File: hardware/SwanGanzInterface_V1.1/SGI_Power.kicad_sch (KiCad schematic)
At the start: 24 parts, among them IC1 LM2937ESX-3.3_NOPB, J1 Conn_01x02_Pin, Q1 SQ2389CES-T1_GE3, SW1 Power_Switch, U1 LM4041CILPR, U2 OPA2350, U3 OPA2350

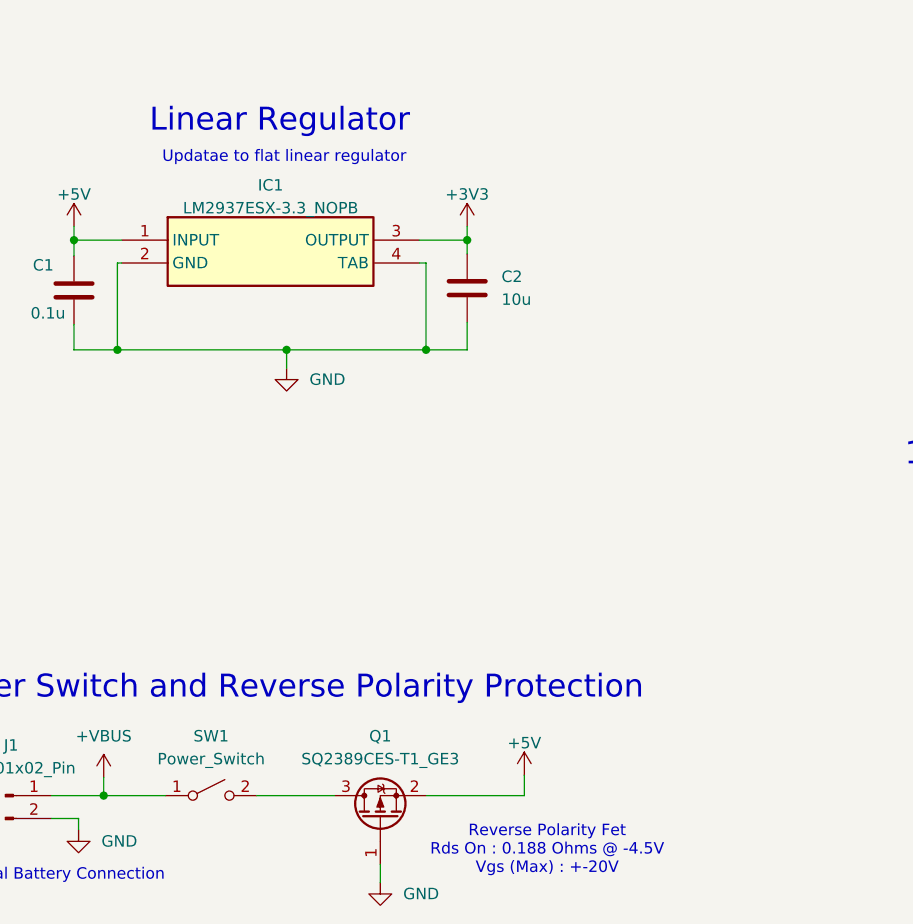
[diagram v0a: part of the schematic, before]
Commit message: Layout work on screen and expanded board size
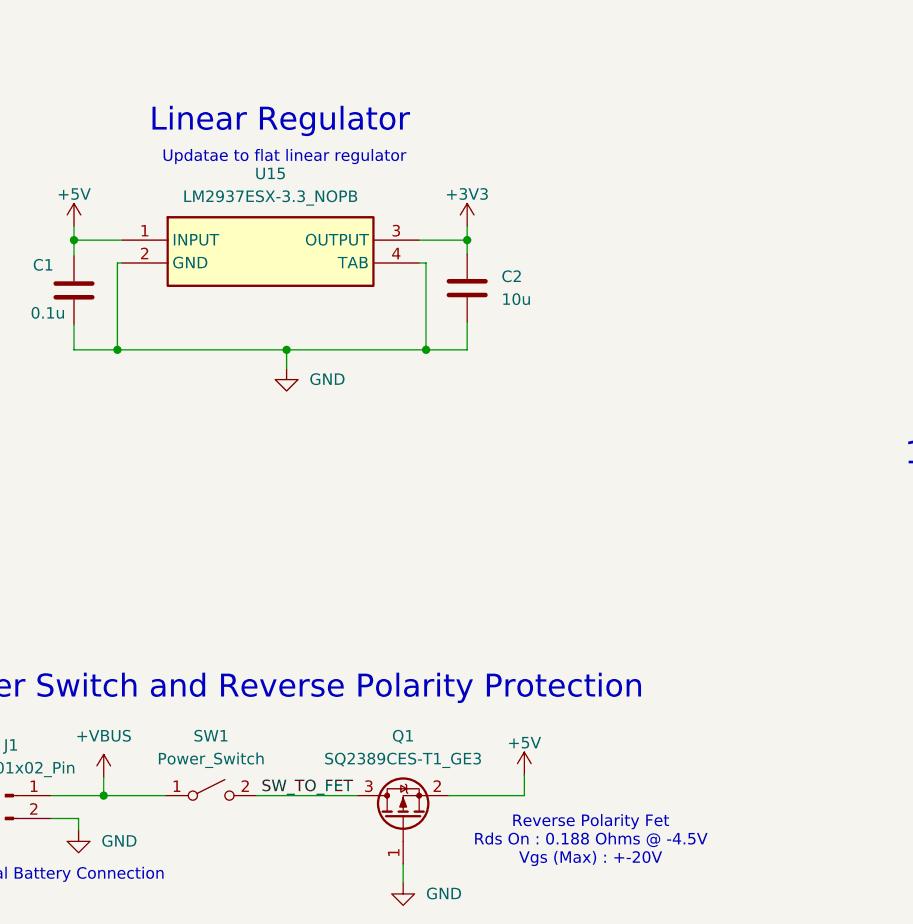
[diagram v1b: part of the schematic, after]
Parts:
- renumbered IC1 to U15
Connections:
- net SW_TO_FET: now reaches Q1.3 (D), SW1.2 (B)
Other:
- moved on the sheet: Q1
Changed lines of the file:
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@@
 	(text "Reverse Polarity Fet\nRds On : 0.188 Ohms @ -4.5V\nVgs (Max) : +-20V"
 		(exclude_from_sim no)
-		(at 89.154 185.674 0)
+		(at 93.98 184.658 0)
 		(effects
 			(font
@@
 	(wire
 		(pts
-			(xy 70.612 189.23) (xy 70.612 187.198)
-		)
-		(stroke
-			(width 0)
-			(type default)
-		)
-	)
-	(wire
-		(pts
 			(xy 232.918 111.252) (xy 235.712 111.252)
 		)
@@
 	(wire
 		(pts
-			(xy 75.692 179.578) (xy 86.614 179.578)
+			(xy 78.232 179.578) (xy 86.614 179.578)
 		)
 		(stroke
@@
 	(wire
 		(pts
-			(xy 56.896 179.578) (xy 65.532 179.578)
+			(xy 56.896 179.578) (xy 68.072 179.578)
 		)
 		(stroke
@@
 	(wire
 		(pts
+			(xy 73.152 187.198) (xy 73.152 189.23)
+		)
+		(stroke
+			(width 0)
+			(type default)
+		)
+	)
+	(wire
+		(pts
 			(xy 150.114 160.528) (xy 157.734 160.528)
 		)
@@
 		)
 	)
-	(global_label "Touch_VRef"
-		(shape output)
-		(at 235.712 111.252 0)
-		(fields_autoplaced yes)
+	(label "SW_TO_FET"
+		(at 57.404 179.578 0)
 		(effects
 			(font
 				(size 1.27 1.27)
 			)
-			(justify left)
-		)
-		(property "Intersheetrefs" "${INTERSHEET_REFS}"
-			(at 249.3409 111.252 0)
-			(effects
-				(font
-					(size 1.27 1.27)
-				)
-				(justify left)
-				(hide yes)
-			)
+			(justify left bottom)
 		)
 	)
@@
 		)
 	)
+	(global_label "Touch_VRef"
+		(shape output)
+		(at 235.712 111.252 0)
+		(fields_autoplaced yes)
+		(effects
+			(font
+				(size 1.27 1.27)
+			)
+			(justify left)
+		)
+		(property "Intersheetrefs" "${INTERSHEET_REFS}"
+			(at 249.3409 111.252 0)
+			(effects
+				(font
+					(size 1.27 1.27)
+				)
+				(justify left)
+				(hide yes)
+			)
+		)
+	)
 	(global_label "+VRef"
 		(shape input)
@@
 	(symbol
 		(lib_id "SGI_SymbolLib:SQ2389CES-T1_GE3")
-		(at 70.612 182.118 90)
+		(at 73.152 182.118 90)
 		(unit 1)
 		(exclude_from_sim no)
@@
 		(dnp no)
 		(property "Reference" "Q1"
-			(at 70.612 172.974 90)
+			(at 73.152 172.974 90)
 			(effects
 				(font
@@
 		)
 		(property "Value" "SQ2389CES-T1_GE3"
-			(at 70.612 175.514 90)
+			(at 73.152 175.514 90)
 			(effects
 				(font
@@
 		)
 		(property "Footprint" "Package_TO_SOT_SMD:SOT-23"
-			(at 72.517 177.038 0)
+			(at 75.057 177.038 0)
 			(effects
 				(font
@@
 		)
 		(property "Datasheet" "kicad-embed://sq2389ces.pdf"
-			(at 74.422 177.038 0)
+			(at 76.962 177.038 0)
 			(effects
 				(font
@@
 		)
 		(property "Description" "-0.18A Id, -60V Vds, P-Channel MOSFET, SOT-23"
-			(at 70.612 182.118 0)
+			(at 73.152 182.118 0)
 			(effects
 				(font
@@
 	(symbol
 		(lib_id "power:GNDA")
-		(at 70.612 189.23 0)
+		(at 73.152 189.23 0)
 		(unit 1)
 		(exclude_from_sim no)
@@
 		(fields_autoplaced yes)
 		(property "Reference" "#PWR04"
-			(at 70.612 195.58 0)
+			(at 73.152 195.58 0)
 			(effects
 				(font
@@
 		)
 		(property "Value" "GND"
-			(at 73.152 190.4999 0)
+			(at 75.692 190.4999 0)
 			(effects
 				(font
@@
 		)
 		(property "Footprint" ""
-			(at 70.612 189.23 0)
+			(at 73.152 189.23 0)
 			(effects
 				(font
@@
 		)
 		(property "Datasheet" ""
-			(at 70.612 189.23 0)
+			(at 73.152 189.23 0)
 			(effects
 				(font
@@
 		)
 		(property "Description" "Power symbol creates a global label with name \"GNDA\" , analog ground"
-			(at 70.612 189.23 0)
+			(at 73.152 189.23 0)
 			(effects
 				(font
@@
 		(dnp no)
 		(fields_autoplaced yes)
-		(property "Reference" "IC1"
-			(at 58.42 111.76 0)
+		(property "Reference" "U15"
+			(at 58.42 110.49 0)
 			(effects
 				(font
@@
 		)
 		(property "Value" "LM2937ESX-3.3_NOPB"
-			(at 58.42 114.3 0)
+			(at 58.42 113.03 0)
 			(effects
 				(font
@@
 			(project ""
 				(path "/4e9a6e30-f660-472b-9696-bea1f34b4545/090a1e64-9482-4912-b352-6eea35714559"
-					(reference "IC1")
+					(reference "U15")
 					(unit 1)
 				)

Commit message: SGI v2 Layout Complete
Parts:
- renumbered U15 to U1, U1 to U2, U2 to U3, U3 to U4
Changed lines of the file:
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@@
 		(on_board yes)
 		(dnp no)
-		(property "Reference" "U3"
+		(property "Reference" "U4"
 			(at 223.266 86.36 0)
 			(effects
@@
 			(project ""
 				(path "/4e9a6e30-f660-472b-9696-bea1f34b4545/090a1e64-9482-4912-b352-6eea35714559"
-					(reference "U3")
+					(reference "U4")
 					(unit 1)
 				)
@@
 		(dnp no)
 		(fields_autoplaced yes)
-		(property "Reference" "#PWR01"
+		(property "Reference" "#PWR02"
 			(at 37.084 189.738 0)
 			(effects
@@
 			(project "SwanGanzInterface_V1.1"
 				(path "/4e9a6e30-f660-472b-9696-bea1f34b4545/090a1e64-9482-4912-b352-6eea35714559"
-					(reference "#PWR01")
+					(reference "#PWR02")
 					(unit 1)
 				)
@@
 		(dnp no)
 		(fields_autoplaced yes)
-		(property "Reference" "U2"
+		(property "Reference" "U3"
 			(at 222.758 60.071 0)
 			(effects
@@
 			(project ""
 				(path "/4e9a6e30-f660-472b-9696-bea1f34b4545/090a1e64-9482-4912-b352-6eea35714559"
-					(reference "U2")
+					(reference "U3")
 					(unit 2)
 				)
@@
 		(dnp no)
 		(fields_autoplaced yes)
-		(property "Reference" "#PWR02"
+		(property "Reference" "#PWR03"
 			(at 39.878 181.356 0)
 			(effects
@@
 			(project ""
 				(path "/4e9a6e30-f660-472b-9696-bea1f34b4545/090a1e64-9482-4912-b352-6eea35714559"
-					(reference "#PWR02")
+					(reference "#PWR03")
 					(unit 1)
 				)
@@
 		(dnp no)
 		(fields_autoplaced yes)
-		(property "Reference" "U1"
+		(property "Reference" "U2"
 			(at 152.654 170.8784 0)
 			(effects
@@
 			(project ""
 				(path "/4e9a6e30-f660-472b-9696-bea1f34b4545/090a1e64-9482-4912-b352-6eea35714559"
-					(reference "U1")
+					(reference "U2")
 					(unit 1)
 				)
@@
 		(dnp no)
 		(fields_autoplaced yes)
-		(property "Reference" "#PWR04"
+		(property "Reference" "#PWR05"
 			(at 73.152 195.58 0)
 			(effects
@@
 			(project "SwanGanzInterface"
 				(path "/4e9a6e30-f660-472b-9696-bea1f34b4545/090a1e64-9482-4912-b352-6eea35714559"
-					(reference "#PWR04")
+					(reference "#PWR05")
 					(unit 1)
 				)
@@
 		(dnp no)
 		(fields_autoplaced yes)
-		(property "Reference" "U15"
+		(property "Reference" "U1"
 			(at 58.42 110.49 0)
 			(effects
@@
 			(project ""
 				(path "/4e9a6e30-f660-472b-9696-bea1f34b4545/090a1e64-9482-4912-b352-6eea35714559"
-					(reference "U15")
+					(reference "U1")
 					(unit 1)
 				)
@@
 		(on_board yes)
 		(dnp no)
-		(property "Reference" "#PWR03"
+		(property "Reference" "#PWR01"
 			(at 36.576 120.142 0)
 			(effects
@@
 			(project "SwanGanzInterface"
 				(path "/4e9a6e30-f660-472b-9696-bea1f34b4545/090a1e64-9482-4912-b352-6eea35714559"
-					(reference "#PWR03")
+					(reference "#PWR01")
 					(unit 1)
 				)
@@
 		(on_board yes)
 		(dnp no)
-		(property "Reference" "#PWR06"
+		(property "Reference" "#PWR07"
 			(at 86.614 181.102 0)
 			(effects
@@
 			(project "SwanGanzInterface"
 				(path "/4e9a6e30-f660-472b-9696-bea1f34b4545/090a1e64-9482-4912-b352-6eea35714559"
-					(reference "#PWR06")
+					(reference "#PWR07")
 					(unit 1)
 				)
@@
 		(on_board yes)
 		(dnp no)
-		(property "Reference" "U3"
+		(property "Reference" "U4"
 			(at 225.552 105.41 0)
 			(effects
@@
 			(project ""
 				(path "/4e9a6e30-f660-472b-9696-bea1f34b4545/090a1e64-9482-4912-b352-6eea35714559"
-					(reference "U3")
+					(reference "U4")
 					(unit 2)
 				)
@@
 		(on_board yes)
 		(dnp no)
-		(property "Reference" "U2"
+		(property "Reference" "U3"
 			(at 266.065 61.9759 0)
 			(effects
@@
 			(project ""
 				(path "/4e9a6e30-f660-472b-9696-bea1f34b4545/090a1e64-9482-4912-b352-6eea35714559"
-					(reference "U2")
+					(reference "U3")
 					(unit 3)
 				)
@@
 		(on_board yes)
 		(dnp no)
-		(property "Reference" "#PWR07"
+		(property "Reference" "#PWR06"
 			(at 80.264 120.142 0)
 			(effects
@@
 			(project "SwanGanzInterface"
 				(path "/4e9a6e30-f660-472b-9696-bea1f34b4545/090a1e64-9482-4912-b352-6eea35714559"
-					(reference "#PWR07")
+					(reference "#PWR06")
 					(unit 1)
 				)
@@
 		(on_board yes)
 		(dnp no)
-		(property "Reference" "U3"
+		(property "Reference" "U4"
 			(at 266.192 96.7739 0)
 			(effects
@@
 			(project ""
 				(path "/4e9a6e30-f660-472b-9696-bea1f34b4545/090a1e64-9482-4912-b352-6eea35714559"
-					(reference "U3")
+					(reference "U4")
 					(unit 3)
 				)
@@
 		(dnp no)
 		(fields_autoplaced yes)
-		(property "Reference" "#PWR05"
+		(property "Reference" "#PWR04"
 			(at 60.198 138.43 0)
 			(effects
@@
 			(project ""
 				(path "/4e9a6e30-f660-472b-9696-bea1f34b4545/090a1e64-9482-4912-b352-6eea35714559"
-					(reference "#PWR05")
+					(reference "#PWR04")
 					(unit 1)
 				)
@@
 		(dnp no)
 		(fields_autoplaced yes)
-		(property "Reference" "U2"
+		(property "Reference" "U3"
 			(at 222.758 38.354 0)
 			(effects
@@
 			(project ""
 				(path "/4e9a6e30-f660-472b-9696-bea1f34b4545/090a1e64-9482-4912-b352-6eea35714559"
-					(reference "U2")
-					(unit 1)
-				)
+					(reference "U3")
+					(unit 1)
+				)
